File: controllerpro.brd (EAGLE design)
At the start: 100 x 80 mm, 10 parts, among them IC1 MCP1703CB, IC2 741G3157DBVR, IC3 741G3157DBVR, IC4 741G3157DBVR, IC5 741G3157DBVR

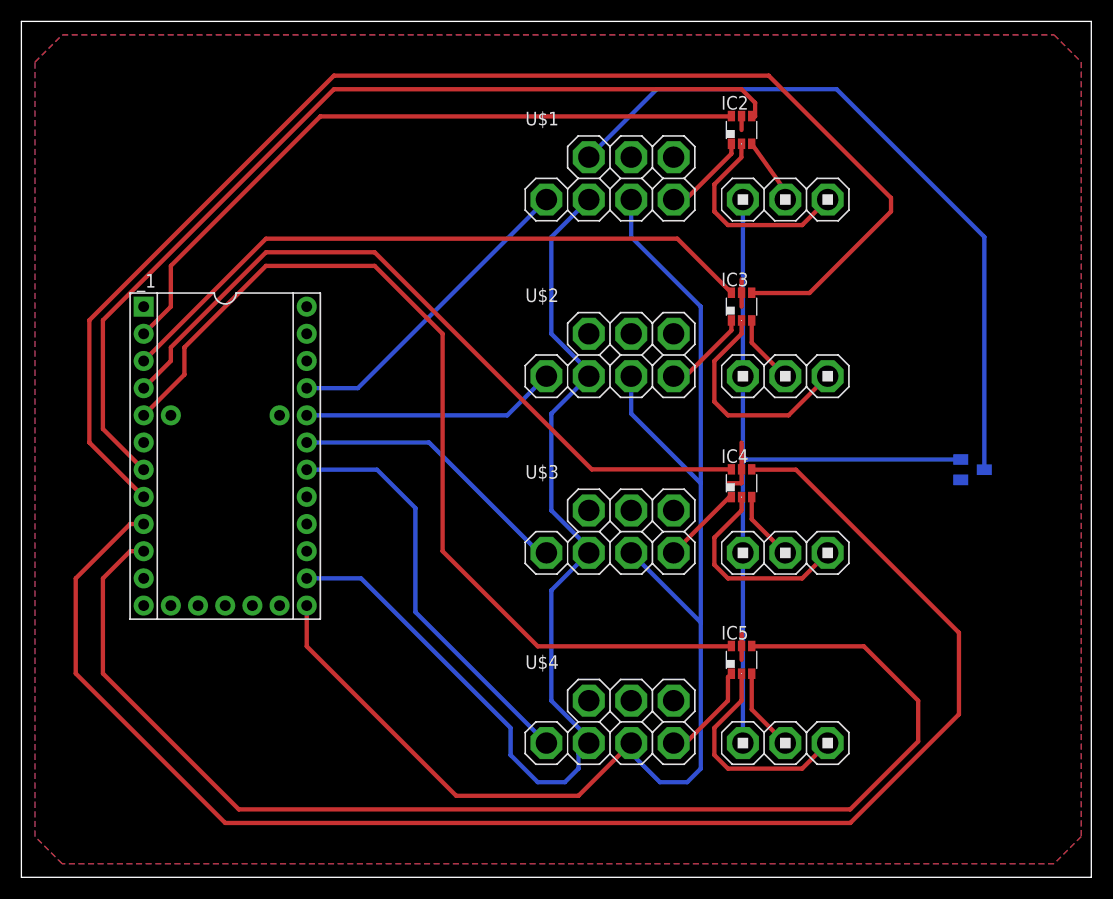
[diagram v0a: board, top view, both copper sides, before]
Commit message: Now smaller!  Rearranged things to minimize size
Mostly to reduce board cost, but hey!
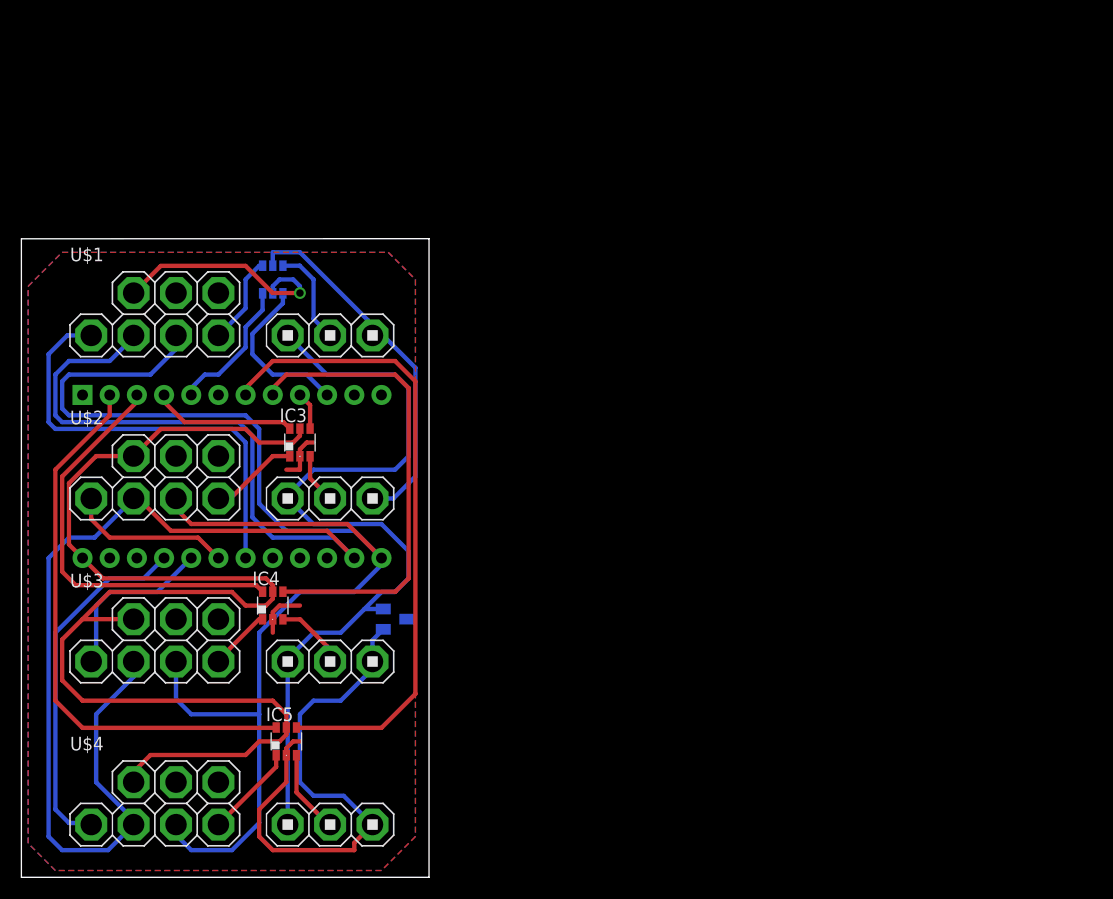
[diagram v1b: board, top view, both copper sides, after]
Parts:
- removed _1: TEENSY, teensy:TEENSY
- added U$5: TEENSY_HEADERS, teensy:TEENSY_HEADERS
- moved IC1 55.8 mm to (34.9, 24.1)
- moved IC2 46.0 mm to (23.5, 55.9), flipped to the bottom, turned to 180 degrees
- moved IC4 45.3 mm to (23.5, 25.4)
- moved U$1 44.4 mm to (18.4, 54.6)
- moved U$2 44.1 mm to (18.4, 39.4)
- moved U$3 43.7 mm to (18.4, 24.1)
- moved IC5 43.2 mm to (24.8, 12.7)
- moved U$4 43.2 mm to (18.4, 8.89)
- moved IC3 43.2 mm to (26.0, 40.6)
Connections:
- net N$11 renamed V33
- net DATA0: now also U$5.D3; no longer _1.D0
- net DATA1: now also U$5.D2; no longer _1.D1
- net DATA2: now also U$5.D1; no longer _1.D2
- net DATA3: now also U$5.D0; no longer _1.D3
- net N$1: now also U$5.D7; no longer _1.D7
- net N$2: now also U$5.D6; no longer _1.D6
- net N64_OR_NES0: now also U$5.B3; no longer _1.B0
- net N64_OR_NES1: now also U$5.B2; no longer _1.B1
- net N64_OR_NES2: now also U$5.B1; no longer _1.B2
- net N64_OR_NES3: now also U$5.B0; no longer _1.B3
- net S_OR_NES0: now also U$5.F7; no longer _1.F4
- net S_OR_NES1: now also U$5.F6; no longer _1.F5
- net S_OR_NES2: now also U$5.F5; no longer _1.F6
- net S_OR_NES3: now also U$5.F4; no longer _1.F7
- net VCC: now also U$5.+5V; no longer _1.+5V
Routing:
- net DATA1: track 125.2 -> 3.54 mm
- net DATA2: track 143.2 -> 44.4 mm
- net DATA0: track 87.6 -> 15.4 mm
- net VCC: track 78.5 -> 146.8 mm, vias 0 -> 1
- net DATA3: track 119.3 -> 60.0 mm
- net N64_OR_NES0: track 65.6 -> 13.0 mm
- net N64_OR_NES1: track 61.8 -> 13.4 mm
- net N$1: track 97.6 -> 137.5 mm
- net N64_OR_NES3: track 88.8 -> 52.4 mm
- net N64_OR_NES2: track 69.3 -> 38.9 mm
- net GND: track 81.0 -> 95.0 mm
- net S_OR_NES0: track 29.7 -> 41.1 mm
- net S_OR_NES2: track 26.7 -> 16.2 mm
- net V33: track 71.3 -> 80.4 mm
- net S_OR_NES1: track 23.9 -> 15.3 mm
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- added copper zone on layer 1, net GND
- added copper zone on layer 16, net VCC
- removed copper zone on layer 16, net GND
- removed copper zone on layer 1, net VCC
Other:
- board size 100 x 80 mm -> 38.1 x 59.7 mm

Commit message: Add my custom teensy parts to the custom library
Just removed the unneeded pins, we'll just be using two headers
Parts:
- U$5: device teensy:TEENSY_HEADERS -> custom:TEENSY_HEADERS
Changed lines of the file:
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@@
 <element name="IC4" library="74xx-little-de" package="DBV_R-PDSO-G6" value="741G3157DBVR" x="23.495" y="25.4"/>
 <element name="IC5" library="74xx-little-de" package="DBV_R-PDSO-G6" value="741G3157DBVR" x="24.765" y="12.7"/>
-<element name="U$5" library="teensy" package="TEENSY_HEADERS" value="TEENSY_HEADERS" x="19.685" y="37.465" rot="MR180"/>
+<element name="U$5" library="custom" package="TEENSY_HEADERS" value="TEENSY_HEADERS" x="19.685" y="37.465" rot="MR180"/>
 </elements>
 <signals>

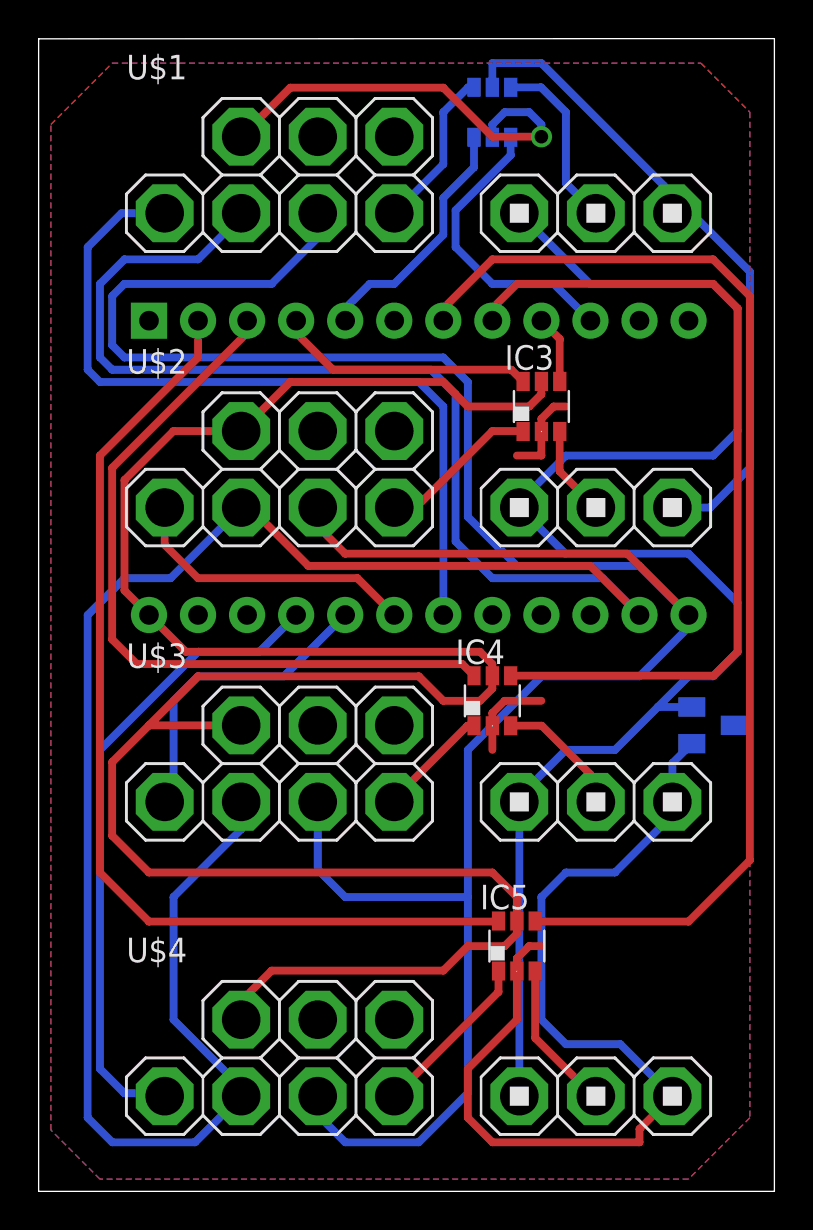
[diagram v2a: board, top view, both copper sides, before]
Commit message: Widening power traces, adding alignment check vias
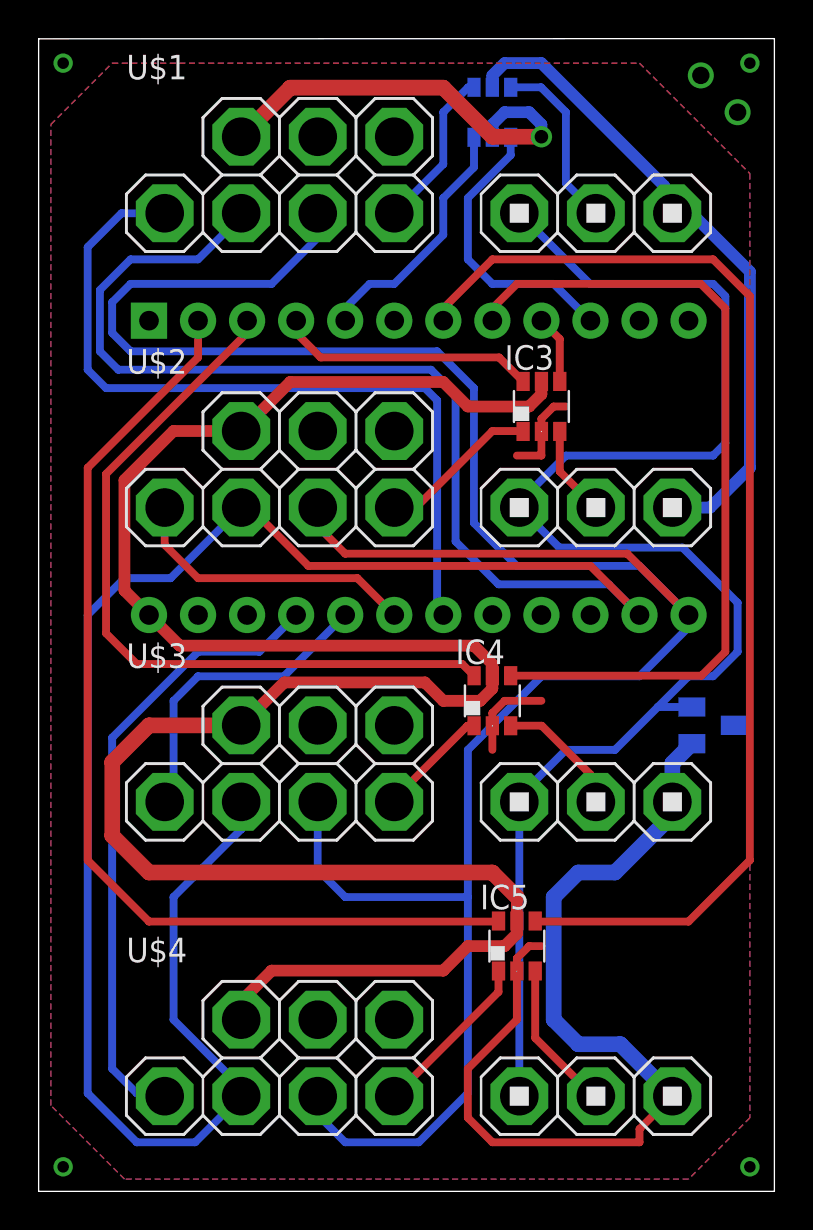
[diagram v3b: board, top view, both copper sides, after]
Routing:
- net VCC: track 146.8 -> 141.8 mm
- net GND: track 95.0 -> 93.3 mm
- net DATA2: track 44.4 -> 43.2 mm
- net N$1: track 137.5 -> 136.4 mm
- net S_OR_NES3: track 33.5 -> 32.6 mm
- net N$2: track 132.2 -> 131.7 mm
- net V33: track 80.4 -> 79.8 mm
- net N64_OR_NES3: track 52.4 -> 52.9 mm
- net DATA0: track 15.4 -> 14.9 mm

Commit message: Adding some net names, connecting a missing GND
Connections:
- net N$1 renamed CLOCK
- net N$2 renamed LATCH
- net GND: now also U$5.GND
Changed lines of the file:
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@@
 </elements>
 <signals>
-<signal name="N$1">
+<signal name="CLOCK">
 <contactref element="U$1" pad="2"/>
 <contactref element="U$2" pad="2"/>
@@
 <wire x1="29.5275" y1="31.4325" x2="31.115" y2="29.845" width="0.4064" layer="16"/>
 </signal>
-<signal name="N$2">
+<signal name="LATCH">
 <contactref element="U$1" pad="3"/>
 <contactref element="U$2" pad="3"/>
@@
 <wire x1="24.765" y1="12.065" x2="25.4" y2="12.7" width="0.4064" layer="1"/>
 <wire x1="25.4" y1="12.7" x2="26.035" y2="12.7" width="0.4064" layer="1"/>
+<contactref element="U$5" pad="GND"/>
 </signal>
 <signal name="V33">

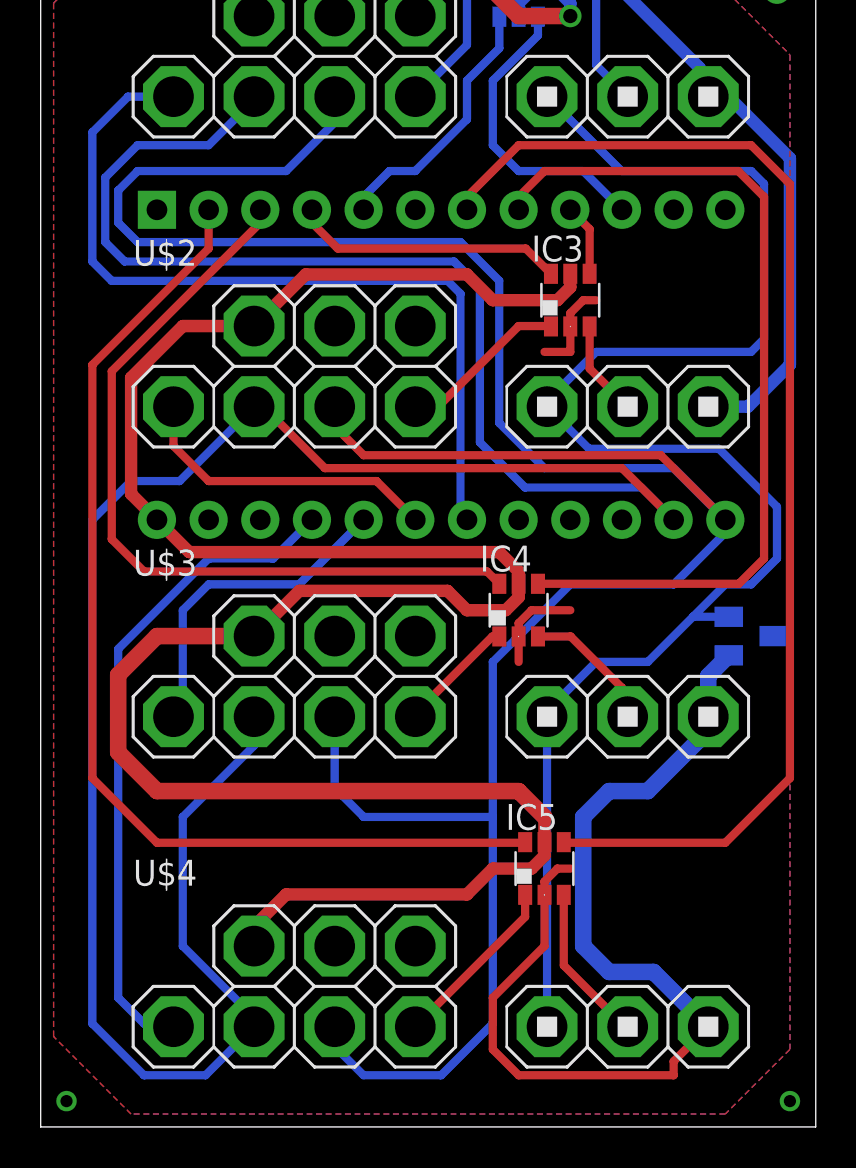
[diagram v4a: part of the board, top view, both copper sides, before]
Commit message: Expanding via mirroring every other controller
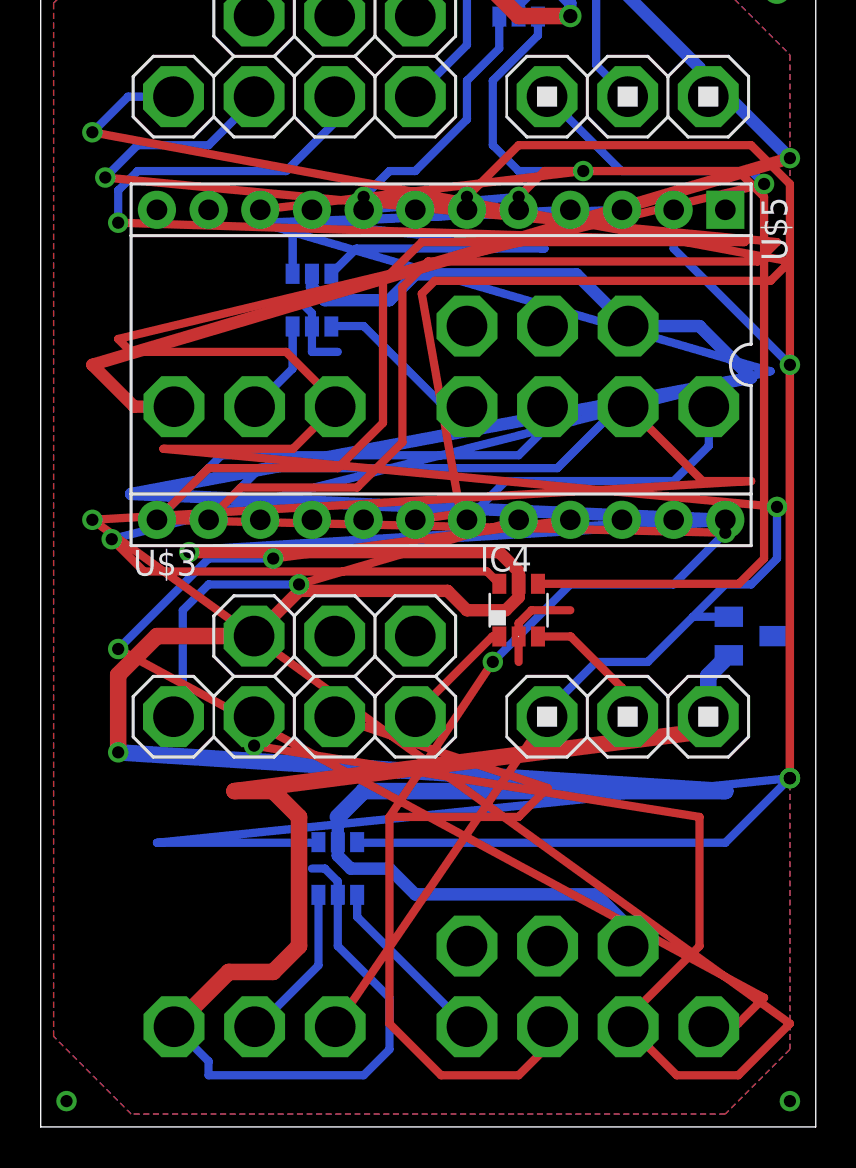
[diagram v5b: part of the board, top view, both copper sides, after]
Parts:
- moved IC3 12.7 mm to (13.3, 40.6), flipped to the bottom
- moved IC5 10.2 mm to (14.6, 12.7), flipped to the bottom
- moved U$2 2.54 mm to (21.0, 39.4), flipped to the bottom
- moved U$4 2.54 mm to (21.0, 8.89), flipped to the bottom
- flipped U$5 to the top
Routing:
- net VCC: track 141.8 -> 245.9 mm, vias 1 -> 3
- net CLOCK: track 136.4 -> 230.9 mm, vias 0 -> 3
- net LATCH: track 131.7 -> 197.5 mm, vias 0 -> 3
- net N64_OR_NES2: track 39.2 -> 97.3 mm, vias 0 -> 1
- net V33: track 79.8 -> 134.4 mm, vias 0 -> 2
- net GND: track 93.3 -> 138.2 mm, vias 0 -> 2
- net S_OR_NES3: track 32.6 -> 63.6 mm, vias 0 -> 2
- net S_OR_NES0: track 41.1 -> 71.5 mm, vias 0 -> 1
- net DATA3: track 60.0 -> 88.8 mm, vias 0 -> 2
- net N64_OR_NES1: track 13.4 -> 35.2 mm
- net DATA0: track 14.9 -> 28.2 mm, vias 0 -> 1
- net N64_OR_NES0: track 13.0 -> 20.0 mm, vias 0 -> 1
- net DATA2: track 43.2 -> 50.2 mm, vias 0 -> 1
- net S_OR_NES2: track 16.2 -> 22.9 mm, vias 0 -> 1
- net N64_OR_NES3: vias 0 -> 2
